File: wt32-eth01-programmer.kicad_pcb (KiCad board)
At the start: 2 copper layers, 31.8 x 76.2 mm, 21 parts, among them J1 USB_C_Receptacle_USB2.0, Q1 BC847, Q2 BC847, SW1 SW_DPST_x2, U1 AMS1117-3.3, U2 CH340G, U3 WT32-ETH0-Board, Y1 12Mhz

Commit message: pcb layout draft
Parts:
- added REF**: MountingHole_2.2mm_M2, MountingHole:MountingHole_2.2mm_M2, F.Cu at (53.3, 47.0)
- added REF**: MountingHole_2.2mm_M2, MountingHole:MountingHole_2.2mm_M2, F.Cu at (80.0, 47.0)
- Q1, Q2: value BC847 -> S8050
- moved Q2 21.7 mm to (61.9, 76.7), turned to 90 degrees
- moved R5 18.6 mm to (64.5, 63.5), turned to 180 degrees
- moved R6 18.3 mm to (65.0, 81.3), turned to 90 degrees
- moved R7 17.9 mm to (65.0, 78.7), turned to 270 degrees
- moved R1 8.80 mm to (64.5, 55.2), turned to 0 degrees
- moved R3 8.80 mm to (64.5, 61.6), turned to 0 degrees
- moved Q1 8.53 mm to (62.0, 81.3), turned to 180 degrees
- moved U1 7.25 mm to (57.9, 57.9), turned to 180 degrees
- moved C2 6.94 mm to (57.4, 64.0)
- moved D1 6.37 mm to (67.3, 55.2), turned to 180 degrees
- moved D3 6.37 mm to (67.3, 61.6), turned to 180 degrees
- moved R2 6.09 mm to (64.5, 58.4), turned to 0 degrees
- moved SW1 5.75 mm to (77.5, 56.5)
- moved C1 5.28 mm to (57.6, 52.8), turned to 180 degrees
- moved U2 4.86 mm to (70.1, 78.2)
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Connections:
- Q1 pad 1: Net-(Q1-Pad1) -> RTS
- Q1 pad 2: RTS -> Net-(Q1-Pad2)
- Q2 pad 1: Net-(Q2-Pad1) -> I00
- Q2 pad 2: I00 -> Net-(Q2-Pad2)
- R6 pad 1: Net-(Q1-Pad1) -> Net-(Q1-Pad2)
- R7 pad 1: Net-(Q2-Pad1) -> Net-(Q2-Pad2)

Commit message: layout
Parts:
- moved C1 1.61 mm to (57.1, 54.4)
- moved C2 1.61 mm to (56.9, 65.5)
- moved C3 1.61 mm to (56.1, 69.1)
- moved U1 1.61 mm to (57.4, 59.4)
- moved Y1 0.54 mm to (72.3, 70.0)

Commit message: routing
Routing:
- net GND: track 0.00 -> 141.6 mm, vias 0 -> 3
- net +3V3: track 0.00 -> 110.9 mm
- net RST: track 0.00 -> 45.5 mm, vias 0 -> 2
- net TX: track 0.00 -> 37.2 mm, vias 0 -> 1
- net D+: track 0.00 -> 33.0 mm, vias 0 -> 2
- net D-: track 0.00 -> 31.5 mm, vias 0 -> 2
- net RX: track 0.00 -> 31.4 mm, vias 0 -> 1
- net DTR: track 0.00 -> 19.0 mm, vias 0 -> 2
- net I00: track 0.00 -> 17.6 mm, vias 0 -> 1
- net +5V: track 0.00 -> 13.9 mm, vias 0 -> 2
- net RTS: track 0.00 -> 9.31 mm
- net Net-(J1-PadA4): track 0.00 -> 7.77 mm
- net Net-(U2-Pad8): track 0.00 -> 6.67 mm
- net Net-(U2-Pad7): track 0.00 -> 5.35 mm
- net CHPD: track 0.00 -> 5.21 mm
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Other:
- net class Power added: clearance 0.3, trace_width 0.5, via_dia 0.8, via_drill 0.4

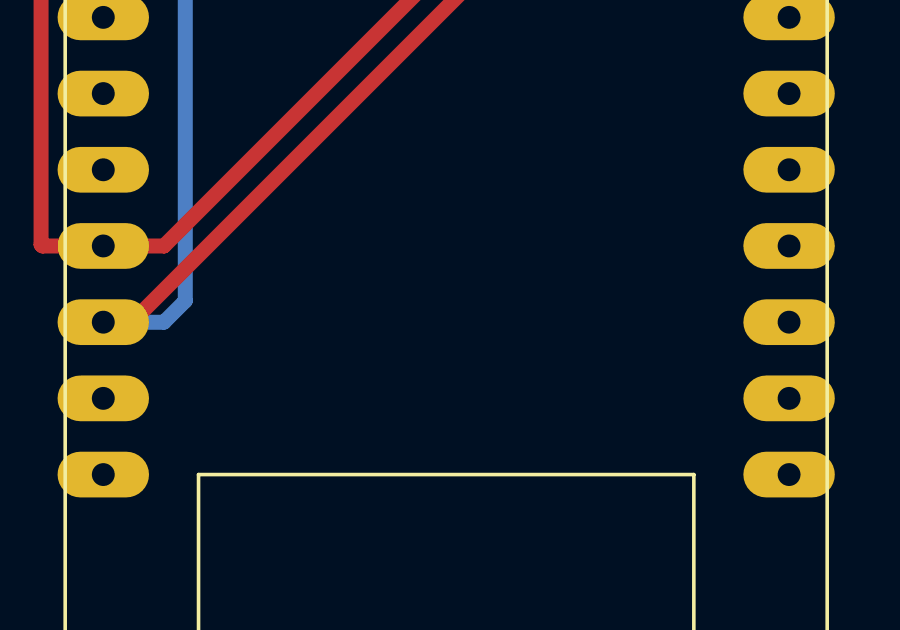
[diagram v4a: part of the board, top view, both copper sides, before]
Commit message: enlarge pads
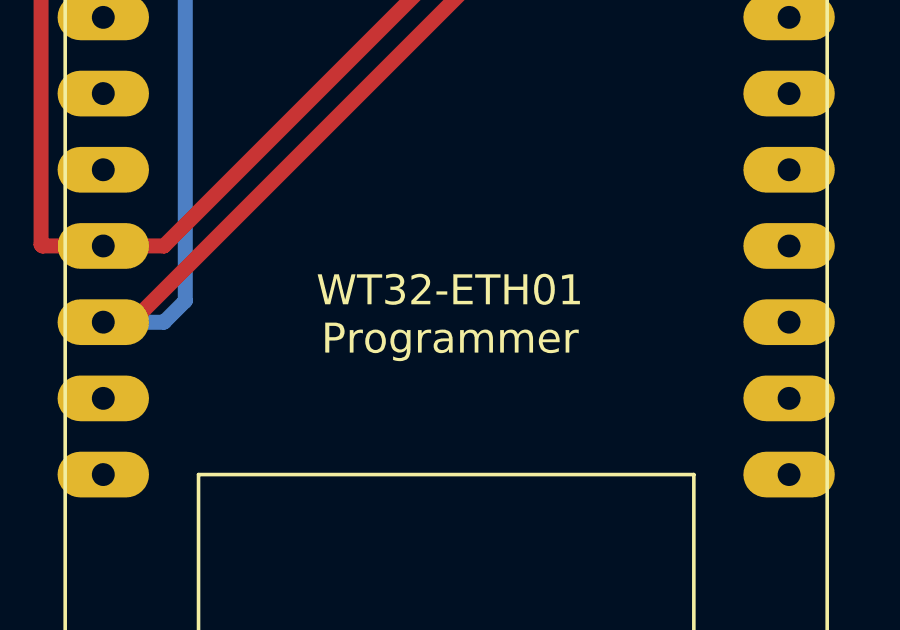
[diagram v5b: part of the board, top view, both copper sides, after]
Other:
- board text added: "WT32-ETH01 Programmer"

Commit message: rearrange tracks
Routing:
- net TX: track 37.2 -> 38.8 mm
- net RX: track 31.4 -> 32.7 mm
- net +3V3: track 110.9 -> 111.6 mm
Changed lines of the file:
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@@
     (thickness 1.6)
     (drawings 12)
-    (tracks 175)
+    (tracks 176)
     (zones 0)
     (modules 23)
@@
   (segment (start 67.629 82.677) (end 67.629 86.16) (width 0.5) (layer F.Cu) (net 3))
   (segment (start 53.221 96.52) (end 55.245 96.52) (width 0.5) (layer F.Cu) (net 3))
-  (segment (start 53.17099 96.46999) (end 53.221 96.52) (width 0.5) (layer F.Cu) (net 3))
-  (segment (start 53.17099 67.73301) (end 53.17099 96.46999) (width 0.5) (layer F.Cu) (net 3))
-  (segment (start 55.372 65.532) (end 53.17099 67.73301) (width 0.5) (layer F.Cu) (net 3))
+  (segment (start 52.324 95.623) (end 53.221 96.52) (width 0.5) (layer F.Cu) (net 3))
+  (segment (start 52.324 68.58) (end 52.324 95.623) (width 0.5) (layer F.Cu) (net 3))
+  (segment (start 55.372 65.532) (end 52.324 68.58) (width 0.5) (layer F.Cu) (net 3))
   (segment (start 65.028 55.245) (end 66.548 55.245) (width 0.25) (layer F.Cu) (net 4))
   (segment (start 65.028 58.42) (end 66.548 58.42) (width 0.25) (layer F.Cu) (net 5))
@@
   (segment (start 72.644 58.42) (end 72.644 63.5) (width 0.25) (layer B.Cu) (net 6))
   (segment (start 77.724 73.279) (end 78.105 73.66) (width 0.25) (layer F.Cu) (net 6))
-  (segment (start 74.76801 80.19299) (end 73.554 81.407) (width 0.25) (layer F.Cu) (net 6))
-  (segment (start 73.554 81.407) (end 72.579 81.407) (width 0.25) (layer F.Cu) (net 6))
-  (segment (start 79.95401 79.190254) (end 78.951274 80.19299) (width 0.25) (layer F.Cu) (net 6))
-  (segment (start 79.95401 75.749746) (end 79.95401 79.190254) (width 0.25) (layer F.Cu) (net 6))
-  (segment (start 78.105 73.900736) (end 79.95401 75.749746) (width 0.25) (layer F.Cu) (net 6))
-  (segment (start 78.951274 80.19299) (end 74.76801 80.19299) (width 0.25) (layer F.Cu) (net 6))
-  (segment (start 78.105 73.66) (end 78.105 73.900736) (width 0.25) (layer F.Cu) (net 6))
   (segment (start 77.724 73.279) (end 78.105 73.66) (width 0.25) (layer B.Cu) (net 6))
   (segment (start 77.724 68.58) (end 77.724 73.279) (width 0.25) (layer B.Cu) (net 6))
+  (segment (start 73.554 81.407) (end 72.579 81.407) (width 0.25) (layer F.Cu) (net 6))
+  (segment (start 79.502 80.01) (end 74.951 80.01) (width 0.25) (layer F.Cu) (net 6))
+  (segment (start 80.518 78.994) (end 79.502 80.01) (width 0.25) (layer F.Cu) (net 6))
+  (segment (start 80.518 74.422) (end 80.518 78.994) (width 0.25) (layer F.Cu) (net 6))
+  (segment (start 74.951 80.01) (end 73.554 81.407) (width 0.25) (layer F.Cu) (net 6))
+  (segment (start 79.756 73.66) (end 80.518 74.422) (width 0.25) (layer F.Cu) (net 6))
+  (segment (start 78.105 73.66) (end 79.756 73.66) (width 0.25) (layer F.Cu) (net 6))
   (segment (start 65.028 61.595) (end 66.548 61.595) (width 0.25) (layer F.Cu) (net 7))
   (segment (start 74.168 80.137) (end 78.105 76.2) (width 0.25) (layer F.Cu) (net 8))
@@
   (segment (start 72.734 61.595) (end 73.369 60.96) (width 0.25) (layer F.Cu) (net 8))
   (segment (start 68.123 61.595) (end 72.734 61.595) (width 0.25) (layer F.Cu) (net 8))
-  (segment (start 79.95401 74.35099) (end 78.105 76.2) (width 0.25) (layer B.Cu) (net 8))
-  (segment (start 79.95401 67.54501) (end 79.95401 74.35099) (width 0.25) (layer B.Cu) (net 8))
-  (segment (start 73.369 60.96) (end 79.95401 67.54501) (width 0.25) (layer B.Cu) (net 8))
+  (segment (start 79.502 76.2) (end 78.105 76.2) (width 0.25) (layer B.Cu) (net 8))
+  (segment (start 80.518 68.109) (end 80.518 75.184) (width 0.25) (layer B.Cu) (net 8))
+  (segment (start 80.518 75.184) (end 79.502 76.2) (width 0.25) (layer B.Cu) (net 8))
+  (segment (start 73.369 60.96) (end 80.518 68.109) (width 0.25) (layer B.Cu) (net 8))
   (segment (start 68.49 50.909998) (end 68.49 51.67) (width 0.25) (layer F.Cu) (net 9))
   (segment (start 66.856002 49.276) (end 68.49 50.909998) (width 0.25) (layer F.Cu) (net 9))
